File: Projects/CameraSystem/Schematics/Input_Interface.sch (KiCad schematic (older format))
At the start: 0 parts

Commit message: feat: set up layout
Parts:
- added C1, C2: 1u, Capacitors_SMD:C_0603_HandSoldering, symbol C
- added J1: 10118192-0001LF, digikey-footprints:USB_Micro_B_Female_10118192, symbol 10118192-0001LF
- added U1: CH340, custom-footprints:SO16, symbol CH340
- added U2: AZ1117CH-3_3TRG1, digikey-footprints:SOT-223, symbol AZ1117CH-3_3TRG1
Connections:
- net labels added: D+, D-, GND, VDD_3V3, VDD_5V0
- wire segments 0 -> 23
- no-connect marks 0 -> 1
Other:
- note added: "ESR < 1.5Ohm"
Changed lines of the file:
@@
 $Descr A4 11693 8268
 encoding utf-8
-Sheet 1 6
+Sheet 2 6
 Title ""
 Date ""
@@
 Comment4 ""
 $EndDescr
-$Sheet
-S 1000 1000 900  650
-U 5BB4C1AE
-F0 "Input_Interface" 60
-F1 "Input_Interface.sch" 60
-F2 "VDD_5V0" O R 1900 1150 60
-F3 "D-" B R 1900 1300 60
-F4 "D+" B R 1900 1450 60
-$EndSheet
-$Sheet
-S 2700 1700 1100 1050
-U 5BB4D99F
-F0 "Microcontroller" 60
-F1 "Microcontroller.sch" 60
-$EndSheet
-$Sheet
-S 4700 900  1100 750
-U 5BB4D9C1
-F0 "Wifi" 60
-F1 "Wifi.sch" 60
-$EndSheet
-$Sheet
-S 4650 2100 1000 800
-U 5BB4DA56
-F0 "Memory" 60
-F1 "Memory.sch" 60
-$EndSheet
-$Sheet
-S 6200 2150 850  800
-U 5BB4DA63
-F0 "Camera" 60
-F1 "Camera.sch" 60
-$EndSheet
+$Comp
+L 10118192-0001LF J1
+U 1 1 5BB4C296
+P 2250 2300
+F 0 "J1" H 2102 2898 60  0000 C CNN
+F 1 "10118192-0001LF" V 2002 2048 60  0000 C CNN
+F 2 "digikey-footprints:USB_Micro_B_Female_10118192" H 2450 2500 60  0001 L CNN
+F 3 "https://cdn.amphenol-icc.com/media/wysiwyg/files/drawing/10118192.pdf" H 2450 2600 60  0001 L CNN
+F 4 "609-4613-1-ND" H 2450 2700 60  0001 L CNN "Digi-Key_PN"
+F 5 "10118192-0001LF" H 2450 2800 60  0001 L CNN "MPN"
+F 6 "Connectors, Interconnects" H 2450 2900 60  0001 L CNN "Category"
+F 7 "USB, DVI, HDMI Connectors" H 2450 3000 60  0001 L CNN "Family"
+F 8 "https://cdn.amphenol-icc.com/media/wysiwyg/files/drawing/10118192.pdf" H 2450 3100 60  0001 L CNN "DK_Datasheet_Link"
+F 9 "/product-detail/en/amphenol-fci/10118192-0001LF/609-4613-1-ND/2785378" H 2450 3200 60  0001 L CNN "DK_Detail_Page"
+F 10 "CONN USB MICRO B RECPT SMT R/A" H 2450 3300 60  0001 L CNN "Description"
+F 11 "Amphenol FCI" H 2450 3400 60  0001 L CNN "Manufacturer"
+F 12 "Active" H 2450 3500 60  0001 L CNN "Status"
+	1    2250 2300
+	1    0    0    -1
+$EndComp
+Wire Wire Line
+	2550 2100 2850 2100
+Wire Wire Line
+	2850 2100 2850 1900
+Wire Wire Line
+	2850 1900 2900 1900
+$Comp
+L GND #PWR01
+U 1 1 5BB4C3EB
+P 2850 3050
+F 0 "#PWR01" H 2850 2800 50  0001 C CNN
+F 1 "GND" H 2850 2900 50  0000 C CNN
+F 2 "" H 2850 3050 50  0001 C CNN
+F 3 "" H 2850 3050 50  0001 C CNN
+	1    2850 3050
+	1    0    0    -1
+$EndComp
+Wire Wire Line
+	2550 2500 2850 2500
+Wire Wire Line
+	2850 2500 2850 3050
+Wire Wire Line
+	2550 2200 2950 2200
+Wire Wire Line
+	2950 2200 2950 2100
+Wire Wire Line
+	2950 2100 3050 2100
+Wire Wire Line
+	2550 2300 3050 2300
+Wire Wire Line
+	2550 2400 2950 2400
+NoConn ~ 3050 2500
+Wire Wire Line
+	2950 2400 2950 2500
+Wire Wire Line
+	2950 2500 3050 2500
+$Comp
+L GND #PWR02
+U 1 1 5BB4C4E7
+P 2150 3050
+F 0 "#PWR02" H 2150 2800 50  0001 C CNN
+F 1 "GND" H 2150 2900 50  0000 C CNN
+F 2 "" H 2150 3050 50  0001 C CNN
+F 3 "" H 2150 3050 50  0001 C CNN
+	1    2150 3050
+	1    0    0    -1
+$EndComp
+Wire Wire Line
+	2150 2900 2150 3050
+Text HLabel 2900 1900 2    60   Output ~ 0
+VDD_5V0
+Text HLabel 3050 2100 2    60   BiDi ~ 0
+D-
+Text HLabel 3050 2300 2    60   BiDi ~ 0
+D+
+$Comp
+L AZ1117CH-3_3TRG1 U2
+U 1 1 5BB4D847
+P 5750 1850
+F 0 "U2" H 5800 2000 60  0000 C CNN
+F 1 "AZ1117CH-3_3TRG1" H 5800 2100 60  0000 C CNN
+F 2 "digikey-footprints:SOT-223" H 5950 2050 60  0001 L CNN
+F 3 "https://www.diodes.com/assets/Datasheets/AZ1117C.pdf" H 5950 2150 60  0001 L CNN
+F 4 "AZ1117CH-3.3TRG1DICT-ND" H 5950 2250 60  0001 L CNN "Digi-Key_PN"
+F 5 "AZ1117CH-3.3TRG1" H 5950 2350 60  0001 L CNN "MPN"
+F 6 "Integrated Circuits (ICs)" H 5950 2450 60  0001 L CNN "Category"
+F 7 "PMIC - Voltage Regulators - Linear" H 5950 2550 60  0001 L CNN "Family"
+F 8 "https://www.diodes.com/assets/Datasheets/AZ1117C.pdf" H 5950 2650 60  0001 L CNN "DK_Datasheet_Link"
+F 9 "/product-detail/en/diodes-incorporated/AZ1117CH-3.3TRG1/AZ1117CH-3.3TRG1DICT-ND/4505206" H 5950 2750 60  0001 L CNN "DK_Detail_Page"
+F 10 "IC REG LINEAR 3.3V 800MA SOT223" H 5950 2850 60  0001 L CNN "Description"
+F 11 "Diodes Incorporated" H 5950 2950 60  0001 L CNN "Manufacturer"
+F 12 "Active" H 5950 3050 60  0001 L CNN "Status"
+	1    5750 1850
+	1    0    0    -1
+$EndComp
+$Comp
+L CH340 U1
+U 1 1 5BB4DB29
+P 4850 3600
+F 0 "U1" H 4850 4100 50  0000 L BNN
+F 1 "CH340" H 4750 3000 50  0000 L BNN
+F 2 "custom-footprints:SO16" H 4750 3250 50  0001 L BNN
+F 3 "Fram" H 4800 3500 50  0001 L BNN
+	1    4850 3600
+	1    0    0    -1
+$EndComp
+Wire Wire Line
+	4750 1850 5450 1850
+Text Label 5100 1850 2    60   ~ 0
+VDD_5V0
+$Comp
+L GND #PWR03
+U 1 1 5BB4DDE6
+P 5750 2600
+F 0 "#PWR03" H 5750 2350 50  0001 C CNN
+F 1 "GND" H 5750 2450 50  0000 C CNN
+F 2 "" H 5750 2600 50  0001 C CNN
+F 3 "" H 5750 2600 50  0001 C CNN
+	1    5750 2600
+	1    0    0    -1
+$EndComp
+Wire Wire Line
+	5750 2250 5750 2600
+Wire Wire Line
+	6150 1950 6300 1950
+Wire Wire Line
+	6300 1950 6300 1850
+Wire Wire Line
+	6150 1850 7000 1850
+Connection ~ 6300 1850
+Text HLabel 7000 1850 2    60   Output ~ 0
+VDD_3V3
+$Comp
+L C C1
+U 1 1 5BB4E02C
+P 5200 2150
+F 0 "C1" H 5225 2250 50  0000 L CNN
+F 1 "1u" H 5225 2050 50  0000 L CNN
+F 2 "Capacitors_SMD:C_0603_HandSoldering" H 5238 2000 50  0001 C CNN
+F 3 "" H 5200 2150 50  0001 C CNN
+	1    5200 2150
+	1    0    0    -1
+$EndComp
+$Comp
+L C C2
+U 1 1 5BB4E099
+P 6500 2150
+F 0 "C2" H 6525 2250 50  0000 L CNN
+F 1 "1u" H 6525 2050 50  0000 L CNN
+F 2 "Capacitors_SMD:C_0603_HandSoldering" H 6538 2000 50  0001 C CNN
+F 3 "" H 6500 2150 50  0001 C CNN
+	1    6500 2150
+	1    0    0    -1
+$EndComp
+Text Notes 6700 2200 0    60   ~ 0
+ESR < 1.5Ohm
+Wire Wire Line
+	5200 2000 5200 1850
+Connection ~ 5200 1850
+Wire Wire Line
+	5200 2300 5200 2450
+Wire Wire Line
+	5200 2450 6500 2450
+Connection ~ 5750 2450
+Wire Wire Line
+	6500 2450 6500 2300
+Wire Wire Line
+	6500 2000 6500 1850
+Connection ~ 6500 1850
 $EndSCHEMATC

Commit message: feat: add schottky diode datasheet
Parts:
- added C? (x2): 22p, Capacitors_SMD:C_0603_HandSoldering, symbol C
- added C? (x3): 100n, Capacitors_SMD:C_0603_HandSoldering, symbol C
- added CUS520: D, symbol D
- added D?: TPD2E001DRLR, digikey-footprints:SOT-553, symbol TPD2E001DRLR
- added F?: MF-MSMF050-2CT-ND 0.5A, symbol Fuse
- added R?: 10k, symbol R
- added Y?: 12MHz, symbol Crystal
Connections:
- net labels added: SPI_RST, SPI_RX, SPI_TX, USB_DN, USB_DP
- net labels removed: D+, D-
- wire segments 23 -> 53
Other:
- note added: "MAIN CONNECTOR"
- note added: "PMIC"
- note added: "USB TO UART"
- moved on the sheet: C1, C2, J1, U1, U2

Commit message: feat:add led datasheets and microcontroler
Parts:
- removed CUS520: D, symbol D
- removed R?: 10k, symbol R
- added D?: APG1608SURKC/T, symbol LED
- added D?: APG1608CGKC/T, symbol LED
- added D?: APG1608SYKC/T, symbol LED
- added R? (x3): 560, symbol R
- added R? (x2): 1k, symbol R
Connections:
- wire segments 53 -> 63
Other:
- moved on the sheet: C?, U1, Y?

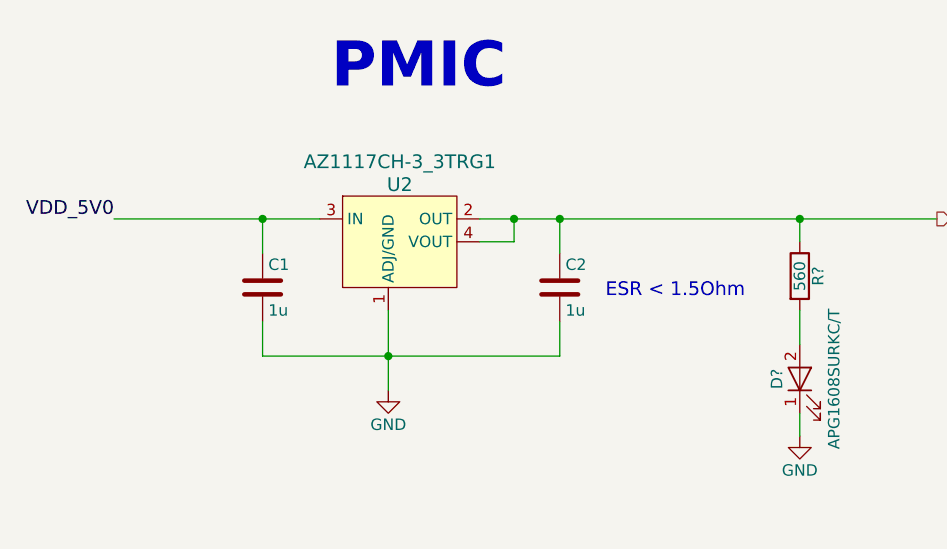
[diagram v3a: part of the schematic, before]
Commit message: feat: add i2c ic, add additional datasheets and simulations
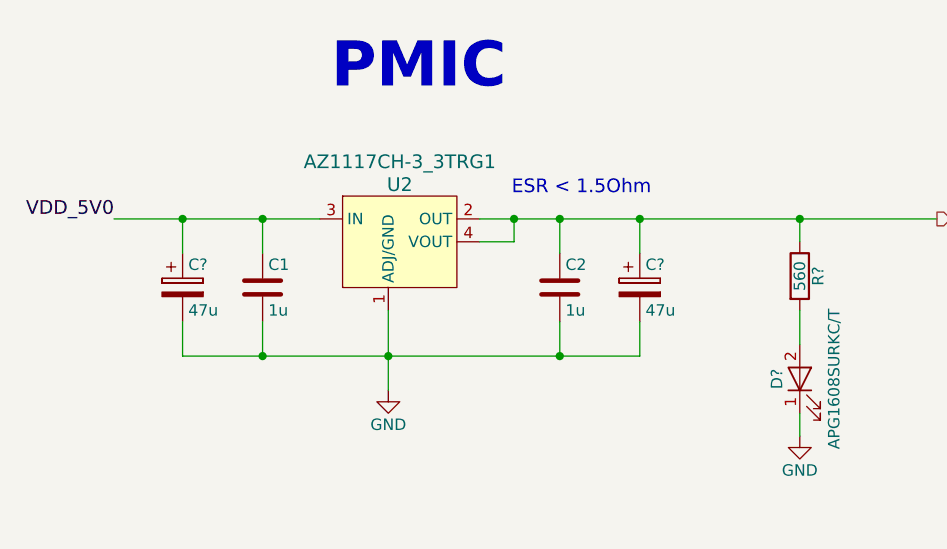
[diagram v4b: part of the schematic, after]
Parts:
- added C? (x2): 47u, symbol CP
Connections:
- net GND: now also C?.2, C?.2
- net VDD_3V3: now also C?.1
- net VDD_5V0: now also C?.1
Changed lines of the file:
@@
 $Descr A4 11693 8268
 encoding utf-8
-Sheet 2 6
+Sheet 2 7
 Title ""
 Date ""
@@
 	1    0    0    -1
 $EndComp
-Text Notes 8850 2250 0    60   ~ 0
+Text Notes 9050 1800 2    60   ~ 0
 ESR < 1.5Ohm
 $Comp
@@
 	7350 2350 7350 2500
 Wire Wire Line
-	7350 2500 8650 2500
+	7000 2500 9000 2500
 Connection ~ 7900 2500
 Wire Wire Line
@@
 	8550 4200 8650 4200
 Connection ~ 5450 5350
+$Comp
+L CP C?
+U 1 1 5BB91E38
+P 9000 2200
+F 0 "C?" H 9025 2300 50  0000 L CNN
+F 1 "47u" H 9025 2100 50  0000 L CNN
+F 2 "" H 9038 2050 50  0001 C CNN
+F 3 "" H 9000 2200 50  0001 C CNN
+	1    9000 2200
+	1    0    0    -1
+$EndComp
+Wire Wire Line
+	9000 1900 9000 2050
+Connection ~ 9000 1900
+Wire Wire Line
+	9000 2500 9000 2350
+Connection ~ 8650 2500
+$Comp
+L CP C?
+U 1 1 5BB9202A
+P 7000 2200
+F 0 "C?" H 7025 2300 50  0000 L CNN
+F 1 "47u" H 7025 2100 50  0000 L CNN
+F 2 "" H 7038 2050 50  0001 C CNN
+F 3 "" H 7000 2200 50  0001 C CNN
+	1    7000 2200
+	1    0    0    -1
+$EndComp
+Wire Wire Line
+	7000 1900 7000 2050
+Connection ~ 7000 1900
+Wire Wire Line
+	7000 2350 7000 2500
+Connection ~ 7350 2500
 $EndSCHEMATC
